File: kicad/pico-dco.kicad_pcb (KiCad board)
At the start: 2 copper layers, 100 x 165 mm, 164 parts, among them Q1 2N3904, Q2 2N3904, Q3 2N3904, Q4 2N3904, Q5 2N3904, Q6 2N3904, U1 L78L05_TO92, U2 TL074, U3 H11L1, U4 TL074, U5 TL074, U6 TL074, U7 TL074, U8 TL074

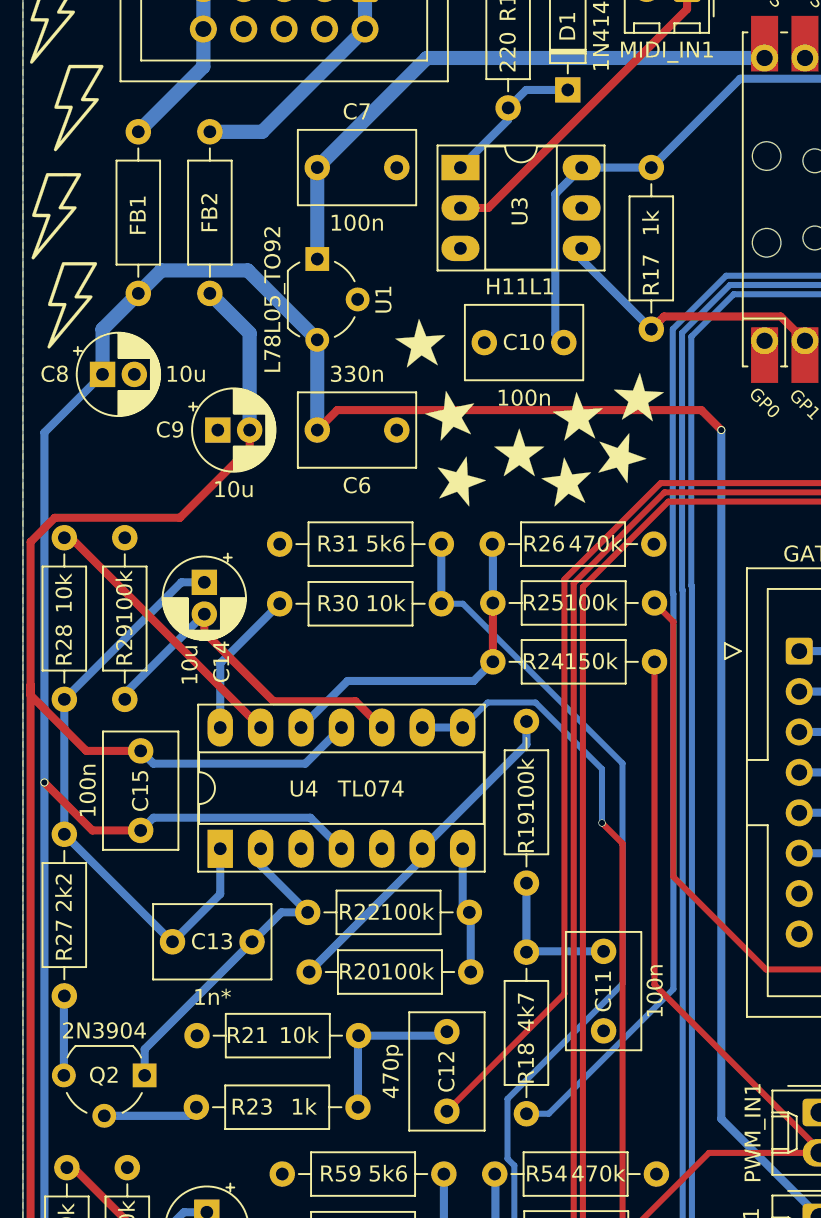
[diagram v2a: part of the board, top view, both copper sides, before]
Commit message: Changed 5V regulator to L7805
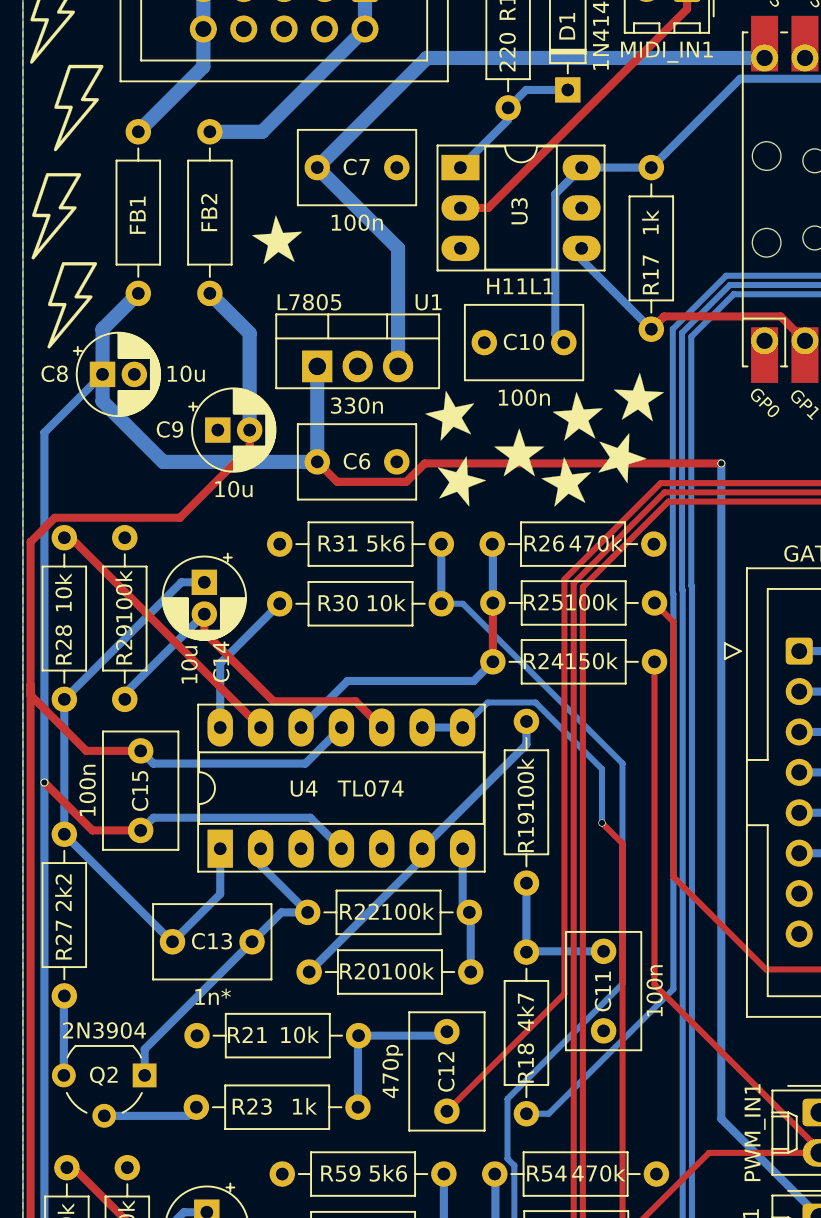
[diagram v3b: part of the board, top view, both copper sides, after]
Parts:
- U1: value L78L05_TO92 -> L7805; footprint Package_TO_SOT_THT:TO-92_Wide -> Package_TO_SOT_THT:TO-220-3_Vertical
- moved G*** 11.1 mm to (66.0, 42.0)
- moved U1 6.75 mm to (68.5, 50.0), turned to 0 degrees
- moved C6 2.00 mm to (73.5, 56.0)
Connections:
- U1 pad 1: +5V -> +12V
- U1 pad 3: +12V -> +5V
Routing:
- net +5V: track 36.7 -> 45.6 mm
- net +12V: track 545.3 -> 546.6 mm
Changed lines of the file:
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@@
     (thickness 1.6)
     (drawings 7)
-    (tracks 740)
+    (tracks 741)
     (zones 0)
     (modules 164)
@@
   )
   (setup
-    (last_trace_width 0.25)
+    (last_trace_width 0.889)
     (user_trace_width 0.381)
     (user_trace_width 0.508)
@@
     (add_net RX)
   )
+  (module Package_TO_SOT_THT:TO-220-3_Vertical (layer F.Cu)
+    (at 68.5 50)
+    (descr "TO-220-3, Vertical, RM 2.54mm, see https://www.vishay.com/docs/66542/to-220-1.pdf")
+    (tags "TO-220-3 Vertical RM 2.54mm")
+    (fp_text reference U1 (at 7 -4) (layer F.SilkS)
+      (effects (font (size 1 1) (thickness 0.15)))
+    )
+    (fp_text value L7805 (at -0.5 -4) (layer F.SilkS)
+      (effects (font (size 1 1) (thickness 0.15)))
+    )
+    (fp_text user %R (at 7 2.5) (layer F.Fab) hide
+      (effects (font (size 1 1) (thickness 0.15)))
+    )
+    (fp_line (start -2.46 -3.15) (end -2.46 1.25) (layer F.Fab) (width 0.1))
+    (fp_line (start -2.46 1.25) (end 7.54 1.25) (layer F.Fab) (width 0.1))
+    (fp_line (start 7.54 1.25) (end 7.54 -3.15) (layer F.Fab) (width 0.1))
+    (fp_line (start 7.54 -3.15) (end -2.46 -3.15) (layer F.Fab) (width 0.1))
+    (fp_line (start -2.46 -1.88) (end 7.54 -1.88) (layer F.Fab) (width 0.1))
+    (fp_line (start 0.69 -3.15) (end 0.69 -1.88) (layer F.Fab) (width 0.1))
+    (fp_line (start 4.39 -3.15) (end 4.39 -1.88) (layer F.Fab) (width 0.1))
+    (fp_line (start -2.58 -3.27) (end 7.66 -3.27) (layer F.SilkS) (width 0.12))
+    (fp_line (start -2.58 1.371) (end 7.66 1.371) (layer F.SilkS) (width 0.12))
+    (fp_line (start -2.58 -3.27) (end -2.58 1.371) (layer F.SilkS) (width 0.12))
+    (fp_line (start 7.66 -3.27) (end 7.66 1.371) (layer F.SilkS) (width 0.12))
+    (fp_line (start -2.58 -1.76) (end 7.66 -1.76) (layer F.SilkS) (width 0.12))
+    (fp_line (start 0.69 -3.27) (end 0.69 -1.76) (layer F.SilkS) (width 0.12))
+    (fp_line (start 4.391 -3.27) (end 4.391 -1.76) (layer F.SilkS) (width 0.12))
+    (fp_line (start -2.71 -3.4) (end -2.71 1.51) (layer F.CrtYd) (width 0.05))
+    (fp_line (start -2.71 1.51) (end 7.79 1.51) (layer F.CrtYd) (width 0.05))
+    (fp_line (start 7.79 1.51) (end 7.79 -3.4) (layer F.CrtYd) (width 0.05))
+    (fp_line (start 7.79 -3.4) (end -2.71 -3.4) (layer F.CrtYd) (width 0.05))
+    (pad 3 thru_hole oval (at 5.08 0) (size 1.905 2) (drill 1.1) (layers *.Cu *.Mask)
+      (net 28 +5V))
+    (pad 2 thru_hole oval (at 2.54 0) (size 1.905 2) (drill 1.1) (layers *.Cu *.Mask)
+      (net 1 GND))
+    (pad 1 thru_hole rect (at 0 0) (size 1.905 2) (drill 1.1) (layers *.Cu *.Mask)
+      (net 57 +12V))
+    (model ${KISYS3DMOD}/Package_TO_SOT_THT.3dshapes/TO-220-3_Vertical.wrl
+      (at (xyz 0 0 0))
+      (scale (xyz 1 1 1))
+      (rotate (xyz 0 0 0))
+    )
+  )
   (module Polykit:star-silk-tiny (layer F.Cu)
-    (at 75 48.5 4)
+    (at 66 42 4)
     (fp_text reference G*** (at 0 0 4) (layer F.SilkS) hide
       (effects (font (size 1.524 1.524) (thickness 0.3)))
@@
     )
   )
-  (module Package_TO_SOT_THT:TO-92_Wide (layer F.Cu)
-    (at 68.5 43.25 270)
-    (descr "TO-92 leads molded, wide, drill 0.75mm (see NXP sot054_po.pdf)")
-    (tags "to-92 sc-43 sc-43a sot54 PA33 transistor")
-    (fp_text reference U1 (at 2.55 -4.19 90) (layer F.SilkS)
-      (effects (font (size 1 1) (thickness 0.15)))
-    )
-    (fp_text value L78L05_TO92 (at 2.54 2.79 90) (layer F.SilkS)
-      (effects (font (size 1 1) (thickness 0.15)))
-    )
-    (fp_line (start 0.74 1.85) (end 4.34 1.85) (layer F.SilkS) (width 0.12))
-    (fp_line (start 0.8 1.75) (end 4.3 1.75) (layer F.Fab) (width 0.1))
-    (fp_line (start -1.01 -3.55) (end 6.09 -3.55) (layer F.CrtYd) (width 0.05))
-    (fp_line (start -1.01 -3.55) (end -1.01 2.01) (layer F.CrtYd) (width 0.05))
-    (fp_line (start 6.09 2.01) (end 6.09 -3.55) (layer F.CrtYd) (width 0.05))
-    (fp_line (start 6.09 2.01) (end -1.01 2.01) (layer F.CrtYd) (width 0.05))
-    (fp_arc (start 2.54 0) (end 4.34 1.85) (angle -20) (layer F.SilkS) (width 0.12))
-    (fp_arc (start 2.54 0) (end 2.54 -2.48) (angle -135) (layer F.Fab) (width 0.1))
-    (fp_arc (start 2.54 0) (end 2.54 -2.48) (angle 135) (layer F.Fab) (width 0.1))
-    (fp_arc (start 2.54 0) (end 3.65 -2.35) (angle 39.71668247) (layer F.SilkS) (width 0.12))
-    (fp_arc (start 2.54 0) (end 1.4 -2.35) (angle -39.12170074) (layer F.SilkS) (width 0.12))
-    (fp_arc (start 2.54 0) (end 0.74 1.85) (angle 20) (layer F.SilkS) (width 0.12))
-    (fp_text user %R (at 2.54 0 90) (layer F.Fab) hide
-      (effects (font (size 1 1) (thickness 0.15)))
-    )
-    (pad 1 thru_hole rect (at 0 0 270) (size 1.5 1.5) (drill 0.8) (layers *.Cu *.Mask)
-      (net 28 +5V))
-    (pad 3 thru_hole circle (at 5.08 0 270) (size 1.5 1.5) (drill 0.8) (layers *.Cu *.Mask)
-      (net 57 +12V))
-    (pad 2 thru_hole circle (at 2.54 -2.54 270) (size 1.5 1.5) (drill 0.8) (layers *.Cu *.Mask)
-      (net 1 GND))
-    (model ${KISYS3DMOD}/Package_TO_SOT_THT.3dshapes/TO-92_Wide.wrl
-      (at (xyz 0 0 0))
-      (scale (xyz 1 1 1))
-      (rotate (xyz 0 0 0))
-    )
-  )
   (module Connector_IDC:IDC-Header_2x05_P2.54mm_Vertical (layer F.Cu)
     (at 71.5 26.25 270)
@@
     (descr "C, Rect series, Radial, pin pitch=5.00mm, , length*width=7.2*4.5mm^2, Capacitor, http://www.wima.com/EN/WIMA_FKS_2.pdf")
     (tags "C Rect series Radial pin pitch 5.00mm  length 7.2mm width 4.5mm Capacitor")
-    (fp_text reference C7 (at 2.5 -3.5) (layer F.SilkS)
+    (fp_text reference C7 (at 2.5 0) (layer F.SilkS)
       (effects (font (size 1 1) (thickness 0.15)))
     )
@@
   )
   (module Capacitor_THT:C_Rect_L7.2mm_W4.5mm_P5.00mm_FKS2_FKP2_MKS2_MKP2 (layer F.Cu)
-    (at 73.5 54 180)
+    (at 73.5 56 180)
     (descr "C, Rect series, Radial, pin pitch=5.00mm, , length*width=7.2*4.5mm^2, Capacitor, http://www.wima.com/EN/WIMA_FKS_2.pdf")
     (tags "C Rect series Radial pin pitch 5.00mm  length 7.2mm width 4.5mm Capacitor")
-    (fp_text reference C6 (at 2.5 -3.5) (layer F.SilkS)
+    (fp_text reference C6 (at 2.5 0) (layer F.SilkS)
       (effects (font (size 1 1) (thickness 0.15)))
     )
@@
   (segment (start 109.4 30.53) (end 109.32 30.61) (width 0.381) (layer B.Cu) (net 24))
   (segment (start 109.4 22.7) (end 109.4 30.53) (width 0.381) (layer B.Cu) (net 24))
-  (segment (start 68.5 43.25) (end 68.5 37.5) (width 0.889) (layer B.Cu) (net 28))
   (segment (start 75.39 30.61) (end 68.5 37.5) (width 0.889) (layer B.Cu) (net 28))
   (segment (start 96.62 30.61) (end 75.39 30.61) (width 0.889) (layer B.Cu) (net 28))
+  (segment (start 73.58 42.58) (end 68.5 37.5) (width 0.889) (layer B.Cu) (net 28))
+  (segment (start 73.58 50) (end 73.58 42.58) (width 0.889) (layer B.Cu) (net 28))
   (segment (start 117.437896 64.07849) (end 111.230501 70.285885) (width 0.381) (layer B.Cu) (net 29))
   (segment (start 122.499839 64.078489) (end 117.437896 64.07849) (width 0.381) (layer B.Cu) (net 29))
@@
   (segment (start 55 47.66) (end 55 50.5) (width 0.889) (layer B.Cu) (net 57))
   (segment (start 57.25 45.41) (end 55 47.66) (width 0.889) (layer B.Cu) (net 57))
-  (segment (start 64.135499 43.965499) (end 68.5 48.33) (width 0.889) (layer B.Cu) (net 57))
-  (segment (start 58.694501 43.965499) (end 64.135499 43.965499) (width 0.889) (layer B.Cu) (net 57))
-  (segment (start 57.25 45.41) (end 58.694501 43.965499) (width 0.889) (layer B.Cu) (net 57))
-  (segment (start 68.5 54) (end 68.5 48.33) (width 0.889) (layer B.Cu) (net 57))
   (segment (start 51.345999 54.154001) (end 51.345999 76.154001) (width 0.508) (layer B.Cu) (net 57))
   (segment (start 55 50.5) (end 51.345999 54.154001) (width 0.508) (layer B.Cu) (net 57))
@@
   (segment (start 148.354001 81.104001) (end 144.904001 81.104001) (width 0.508) (layer F.Cu) (net 57))
   (segment (start 100.1 103.5) (end 93.9 97.3) (width 0.508) (layer B.Cu) (net 57))
-  (segment (start 93.9 97.3) (end 93.9 54) (width 0.508) (layer B.Cu) (net 57))
-  (segment (start 93.9 54) (end 93.9 54) (width 0.508) (layer B.Cu) (net 57))
-  (via (at 93.9 54) (size 0.508) (drill 0.381) (layers F.Cu B.Cu) (net 57))
-  (segment (start 69.754001 52.745999) (end 68.5 54) (width 0.508) (layer F.Cu) (net 57))
-  (segment (start 92.645999 52.745999) (end 69.754001 52.745999) (width 0.508) (layer F.Cu) (net 57))
-  (segment (start 93.9 54) (end 92.645999 52.745999) (width 0.508) (layer F.Cu) (net 57))
+  (segment (start 93.9 97.3) (end 93.9 56.1) (width 0.508) (layer B.Cu) (net 57))
+  (segment (start 58.811 56) (end 55 52.189) (width 0.889) (layer B.Cu) (net 57))
+  (segment (start 55 52.189) (end 55 50.5) (width 0.889) (layer B.Cu) (net 57))
+  (segment (start 68.5 56) (end 58.811 56) (width 0.889) (layer B.Cu) (net 57))
+  (via (at 93.9 56.1) (size 0.508) (drill 0.381) (layers F.Cu B.Cu) (net 57))
+  (segment (start 69.754001 57.254001) (end 68.5 56) (width 0.508) (layer F.Cu) (net 57))
+  (segment (start 74.101921 57.254001) (end 69.754001 57.254001) (width 0.508) (layer F.Cu) (net 57))
+  (segment (start 75.255922 56.1) (end 74.101921 57.254001) (width 0.508) (layer F.Cu) (net 57))
+  (segment (start 93.9 56.1) (end 75.255922 56.1) (width 0.508) (layer F.Cu) (net 57))
+  (segment (start 68.5 56) (end 68.5 50) (width 0.889) (layer B.Cu) (net 57))
   (segment (start 131.949999 82.700001) (end 129.68 84.97) (width 0.508) (layer B.Cu) (net 58))
   (segment (start 141.500001 82.700001) (end 131.949999 82.700001) (width 0.508) (layer B.Cu) (net 58))
